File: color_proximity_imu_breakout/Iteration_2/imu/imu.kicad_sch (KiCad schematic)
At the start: 8 parts, among them J4 Conn_01x05, U6 ICM-20602

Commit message: imu updated iteration 2
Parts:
- added C1, C2: 10u, Capacitor_SMD:C_0603_1608Metric_Pad1.08x0.95mm_HandSolder, symbol Device:C
- added J1, J2: Conn_01x10, pcb_footprints:GT-B0502MSV27-10S1101, symbol Connector_Generic:Conn_01x10
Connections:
- net +3.3V: now also C1.2, C2.2, J1.9 (Pin_9), J2.9 (Pin_9)
- net +5V: now also J1.10 (Pin_10), J2.10 (Pin_10)
- net GND: now also C1.1, C2.1, J1.6 (Pin_6), J2.6 (Pin_6)
- net scl: now also J1.7 (Pin_7), J2.7 (Pin_7)
- net sda: now also J1.8 (Pin_8), J2.8 (Pin_8)
- no-connect marks 1 -> 11

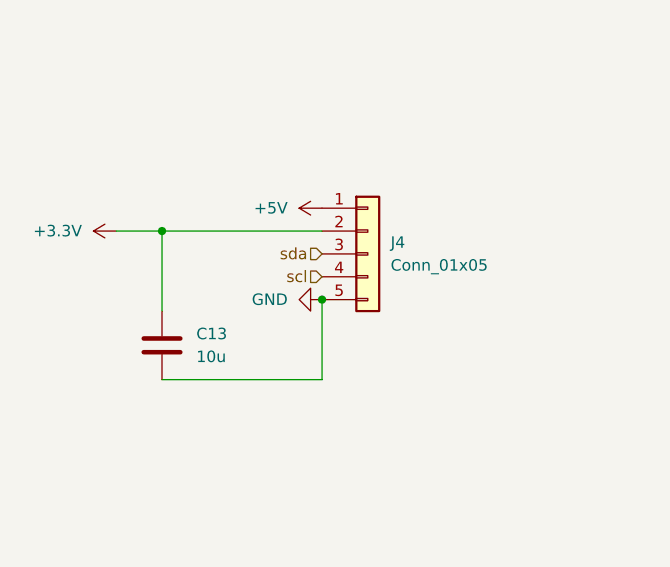
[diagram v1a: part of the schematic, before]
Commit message: finished base board PCB + created production files for base board and modules
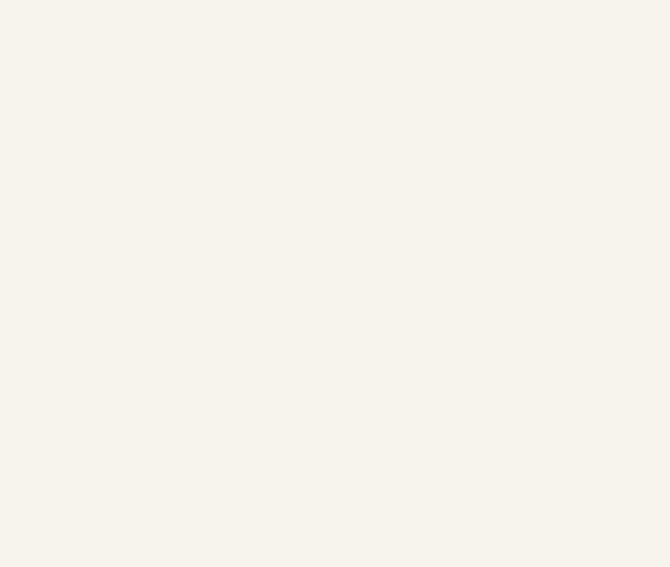
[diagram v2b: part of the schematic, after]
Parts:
- removed C13: 10u, Capacitor_SMD:C_0603_1608Metric_Pad1.08x0.95mm_HandSolder, symbol Device:C
- removed J4: Conn_01x05, Connector_PinHeader_2.54mm:PinHeader_1x05_P2.54mm_Vertical, symbol Connector_Generic:Conn_01x05
- C1, C2: Manufacturer_Name (none) -> Samsung Electro-Mechanics; Manufacturer_Part_Number (none) -> CL10A106KP8NNNC
- C10, C7: Manufacturer_Name (none) -> Samsung Electro-Mechanics; Manufacturer_Part_Number (none) -> CL05B104KB54PNC
- C8: Manufacturer_Name (none) -> Samsung Electro-Mechanics; Manufacturer_Part_Number (none) -> CL10A225KO8NNNC
- C9: Manufacturer_Name (none) -> Samsung Electro-Mechanics; Manufacturer_Part_Number (none) -> CL05B103KB5NNNC
- J1, J2: Manufacturer_Name (none) -> G-Switch; Manufacturer_Part_Number (none) -> GT-B0502MSV27-10S1101
- U6: Manufacturer_Name (none) -> TDK InvenSense

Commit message: updated host schematic and imu production files
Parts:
- U6: footprint Package_LGA:LGA-16_3x3mm_P0.5mm_LayoutBorder3x5y -> pcb_footprints:IAM20680HP
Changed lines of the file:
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@@
 			)
 		)
-		(property "Footprint" "Package_LGA:LGA-16_3x3mm_P0.5mm_LayoutBorder3x5y"
+		(property "Footprint" "pcb_footprints:IAM20680HP"
 			(at 203.2 62.23 0)
 			(effects

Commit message: updated production files
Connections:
- net +5V is gone; now on net GND: J1.10 (Pin_10), J2.10 (Pin_10)
- net +3.3V: now also C1.1, C2.1, J1.7 (Pin_7), J2.7 (Pin_7); no longer C1.2, C2.2, J1.9 (Pin_9), J2.9 (Pin_9)
- net GND: now also C1.2, C2.2; no longer C1.1, C2.1, J1.6 (Pin_6), J2.6 (Pin_6)
- net scl: now also J1.9 (Pin_9), J2.9 (Pin_9); no longer J1.7 (Pin_7), J2.7 (Pin_7)
- no-connect marks 11 -> 13
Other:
- moved on the sheet: C1, C2
